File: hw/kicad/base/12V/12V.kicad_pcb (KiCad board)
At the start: 2 copper layers, 50 x 50 mm, 29 parts, among them J1 USB_B_Micro, J2 TOP, J3 XT60PW-M, J4 BUTTOM, U1 LM1117MP-3.3, U2 LM2596S-5, U3 CP2102N-Axx-xQFN28

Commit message: 修改尺寸至45x45
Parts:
- added D9: LED, LED_SMD:LED_0805_2012Metric, F.Cu at (83.0, 58.8)
- added JUMP1: 0, Resistor_SMD:R_01005_0402Metric, F.Cu at (71.7, 65.7)
- added R5: 10k, Resistor_SMD:R_0805_2012Metric, F.Cu at (80.3, 58.9)
- C1: footprint Capacitor_Tantalum_SMD:CP_EIA-3528-21_Kemet-B -> Capacitor_SMD:C_0805_2012Metric
- C10: value 10uF -> 47uF; footprint Capacitor_Tantalum_SMD:CP_EIA-3528-21_Kemet-B -> Capacitor_Tantalum_SMD:CP_EIA-3216-12_Kemet-S
- C2, C4, C5: footprint Capacitor_SMD:C_0603_1608Metric -> Capacitor_SMD:C_0805_2012Metric
- C6: footprint Capacitor_Tantalum_SMD:CP_EIA-3528-21_Kemet-B -> Capacitor_Tantalum_SMD:CP_EIA-6032-28_Kemet-C
- C9: value 10uF -> 0.1uF; footprint Capacitor_Tantalum_SMD:CP_EIA-3528-21_Kemet-B -> Capacitor_SMD:C_0805_2012Metric
- J1: footprint Connector_USB:USB_Micro-B_Molex_47346-0001 -> Connector_USB:USB_Micro-B_Wuerth_629105150521
- J3: value XT60PW-M -> XT30PW-M; footprint XT:XT60-PW-M -> XT:XT30-PAD
- R1, R2, R3, R4: footprint Resistor_SMD:R_0201_0603Metric -> Resistor_SMD:R_0805_2012Metric
- moved R1 25.0 mm to (83.0, 63.1), turned to 90 degrees
- moved R2 22.1 mm to (80.3, 63.1), turned to -90 degrees
- moved D1 17.5 mm to (78.9, 51.1), turned to -90 degrees
- moved U2 15.6 mm to (62.8, 39.8)
- moved D5 15.1 mm to (66.9, 59.2), turned to -90 degrees
- moved L1 14.8 mm to (79.9, 39.7)
- moved D6 12.1 mm to (69.5, 59.2), turned to -90 degrees
- moved J3 11.9 mm to (49.6, 45.4)
- moved C5 11.5 mm to (92.7, 43.4), turned to 90 degrees
- moved C8 11.1 mm to (62.1, 51.0)
- moved C4 10.8 mm to (74.9, 65.5), turned to 180 degrees
- moved C3 10.1 mm to (71.1, 50.9)
- moved C6 8.99 mm to (89.0, 41.7), turned to 90 degrees
- moved U1 8.47 mm to (89.8, 60.9)
- moved D8 8.13 mm to (85.1, 51.1), turned to 90 degrees
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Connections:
- C4 pad 2: VBUS -> Net-(U3-VBUS)
- J3 pad 1: +BATT -> GND
- J3 pad 2: GND -> +BATT
- U3 pad 7: VBUS -> Net-(U3-VBUS)
- U3 pad 8: VBUS -> Net-(U3-VBUS)
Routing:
- net /ADC_1: track 3.38 -> 36.9 mm
- net +BATT: track 78.4 -> 62.1 mm, vias 14 -> 10
- net +3.3V: track 33.5 -> 46.7 mm
- net /UART1_RX: track 36.7 -> 25.8 mm, vias 2 -> 3
- net Net-(D1-K): track 14.2 -> 21.5 mm
- net /UART1_TX: track 30.8 -> 23.8 mm, vias 2 -> 3
- net Net-(U3-VBUS): track 0.00 -> 6.70 mm
- net +5V: track 77.8 -> 72.6 mm, vias 4 -> 6
- net Net-(D8-A): track 33.0 -> 37.3 mm
- net Net-(D9-K): track 0.00 -> 2.74 mm
- net Net-(J1-D-): track 6.39 -> 8.70 mm
- net Net-(J1-D+): track 6.58 -> 5.15 mm
- net /USB-: track 28.5 -> 29.4 mm, vias 4 -> 2
- net /USB+: track 35.9 -> 36.3 mm, vias 3 -> 2
- net GND: vias 66 -> 40
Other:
- board size 50 x 50 mm -> 45 x 45 mm

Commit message: Pindar v1.0
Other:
- board text added: "Pindar v1.0 Type BASE 12V power v1.0"
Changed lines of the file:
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@@
     (property "ki_keywords" "R res resistor")
     (attr smd)
-    (fp_text reference "R5" (at 0.0544 0.0026 90) (layer "F.SilkS")
+    (fp_text reference "R5" (at 0.0544 0.0026 90) (layer "F.SilkS") hide
         (effects (font (size 1 1) (thickness 0.15)))
     )
@@
     (property "ki_keywords" "cap capacitor")
     (attr smd)
-    (fp_text reference "C5" (at 3.556 0 90) (layer "F.SilkS")
+    (fp_text reference "C5" (at 3.556 0 90) (layer "F.SilkS") hide
         (effects (font (size 1 1) (thickness 0.15)))
     )
@@
     (property "ki_keywords" "cap capacitor")
     (attr smd)
-    (fp_text reference "C2" (at -0.0808 -0.0074 180) (layer "F.SilkS")
+    (fp_text reference "C2" (at -0.0808 -0.0074 180) (layer "F.SilkS") hide
         (effects (font (size 1 1) (thickness 0.15)))
     )
@@
     (property "ki_keywords" "diode Schottky")
     (attr smd)
-    (fp_text reference "D8" (at -0.1016 -0.1016 180) (layer "F.SilkS")
+    (fp_text reference "D8" (at -0.1016 -0.1016 180) (layer "F.SilkS") hide
         (effects (font (size 1 1) (thickness 0.15)))
     )
@@
     (property "ki_keywords" "diode Schottky")
     (attr smd)
-    (fp_text reference "D7" (at -0.0508 -0.2032 90) (layer "F.SilkS")
+    (fp_text reference "D7" (at -0.0508 -0.2032 90) (layer "F.SilkS") hide
         (effects (font (size 1 1) (thickness 0.15)))
     )
@@
     (property "ki_keywords" "cap capacitor")
     (attr smd)
-    (fp_text reference "C6" (at 0 0.0508 90) (layer "F.SilkS")
+    (fp_text reference "C6" (at 0 0.0508 90) (layer "F.SilkS") hide
         (effects (font (size 1 1) (thickness 0.15)))
     )
@@
     (property "ki_keywords" "cap capacitor")
     (attr smd)
-    (fp_text reference "C10" (at -0.0212 0.0508 180) (layer "F.SilkS")
+    (fp_text reference "C10" (at -0.0212 0.0508 180) (layer "F.SilkS") hide
         (effects (font (size 1 1) (thickness 0.15)))
     )
@@
     (property "字段 4" "36V")
     (attr smd)
-    (fp_text reference "C3" (at 2.3952 -2.1172) (layer "F.SilkS")
+    (fp_text reference "C3" (at 2.3952 -2.1172) (layer "F.SilkS") hide
         (effects (font (size 1 1) (thickness 0.15)))
     )
@@
     (property "ki_keywords" "connector")
     (attr smd)
-    (fp_text reference "J2" (at 0 -13.76 90) (layer "F.SilkS")
+    (fp_text reference "J2" (at 0 -13.76 90) (layer "F.SilkS") hide
         (effects (font (size 1 1) (thickness 0.15)))
     )
@@
     (property "ki_keywords" "diode Schottky")
     (attr smd)
-    (fp_text reference "D3" (at -0.3216 -0.0762 -90) (layer "F.SilkS")
+    (fp_text reference "D3" (at -0.3216 -0.0762 -90) (layer "F.SilkS") hide
         (effects (font (size 1 1) (thickness 0.15)))
     )
@@
     (property "ki_keywords" "diode Schottky")
     (attr smd)
-    (fp_text reference "D6" (at -0.0225 -0.0762 90) (layer "F.SilkS")
+    (fp_text reference "D6" (at -0.0225 -0.0762 90) (layer "F.SilkS") hide
         (effects (font (size 1 1) (thickness 0.15)))
     )
@@
     (property "ki_keywords" "LED diode")
     (attr smd)
-    (fp_text reference "D9" (at -0.1755 -0.067 90) (layer "F.SilkS")
+    (fp_text reference "D9" (at -0.1755 -0.067 90) (layer "F.SilkS") hide
         (effects (font (size 1 1) (thickness 0.15)))
     )
@@
     (property "ki_keywords" "diode Schottky")
     (attr smd)
-    (fp_text reference "D4" (at -0.22 -0.0762 90) (layer "F.SilkS")
+    (fp_text reference "D4" (at -0.22 -0.0762 90) (layer "F.SilkS") hide
         (effects (font (size 1 1) (thickness 0.15)))
     )
@@
     (property "ki_keywords" "inductor choke coil reactor magnetic")
     (attr smd)
-    (fp_text reference "L1" (at -0.0398 0.145 90) (layer "F.SilkS")
+    (fp_text reference "L1" (at -0.0398 0.145 90) (layer "F.SilkS") hide
         (effects (font (size 1 1) (thickness 0.15)))
     )
@@
     (property "ki_keywords" "R res resistor")
     (attr smd)
-    (fp_text reference "R2" (at 0.0508 0 90) (layer "F.SilkS")
+    (fp_text reference "R2" (at 0.0508 0 90) (layer "F.SilkS") hide
         (effects (font (size 1 1) (thickness 0.15)))
     )
@@
     (property "ki_keywords" "diode Schottky")
     (attr smd)
-    (fp_text reference "D2" (at -0.2708 -0.0508 90) (layer "F.SilkS")
+    (fp_text reference "D2" (at -0.2708 -0.0508 90) (layer "F.SilkS") hide
         (effects (font (size 1 1) (thickness 0.15)))
     )
@@
     (property "ki_keywords" "USB UART bridge")
     (attr smd)
-    (fp_text reference "U3" (at 0 -3.8) (layer "F.SilkS")
+    (fp_text reference "U3" (at 0 -3.8) (layer "F.SilkS") hide
         (effects (font (size 1 1) (thickness 0.15)))
     )
@@
     (property "ki_keywords" "cap capacitor")
     (attr smd)
-    (fp_text reference "C4" (at -1.5138 -0.0508) (layer "F.SilkS")
+    (fp_text reference "C4" (at -1.5138 -0.0508) (layer "F.SilkS") hide
         (effects (font (size 1 1) (thickness 0.15)))
     )
@@
     (property "ki_keywords" "linear regulator ldo fixed positive")
     (attr smd)
-    (fp_text reference "U1" (at 0.1016 -0.1524) (layer "F.SilkS")
+    (fp_text reference "U1" (at 0.1016 -0.1524) (layer "F.SilkS") hide
         (effects (font (size 1 1) (thickness 0.15)))
     )
@@
     (property "ki_keywords" "diode Schottky")
     (attr smd)
-    (fp_text reference "D1" (at 0.0566 -0.1524 -180) (layer "F.SilkS")
+    (fp_text reference "D1" (at 0.0566 -0.1524 -180) (layer "F.SilkS") hide
         (effects (font (size 1 1) (thickness 0.15)))
     )
@@
     (property "ki_keywords" "cap capacitor")
     (attr smd)
-    (fp_text reference "C1" (at 0.1856 0.0336 90) (layer "F.SilkS")
+    (fp_text reference "C1" (at 0.1856 0.0336 90) (layer "F.SilkS") hide
         (effects (font (size 1 1) (thickness 0.15)))
     )
@@
     (property "ki_keywords" "R res resistor")
     (attr smd)
-    (fp_text reference "R1" (at 0.0508 -0.0092 90) (layer "F.SilkS")
+    (fp_text reference "R1" (at 0.0508 -0.0092 90) (layer "F.SilkS") hide
         (effects (font (size 1 1) (thickness 0.15)))
     )
@@
     (property "ki_keywords" "Step-Down Voltage Regulator 5V 3A")
     (attr smd)
-    (fp_text reference "U2" (at -4.1956 0.0272) (layer "F.SilkS")
+    (fp_text reference "U2" (at -4.1956 0.0272) (layer "F.SilkS") hide
         (effects (font (size 1 1) (thickness 0.15)))
     )
@@
     (property "字段 4" "30V")
     (attr smd)
-    (fp_text reference "C8" (at 2.446 -2.1172 -180) (layer "F.SilkS")
+    (fp_text reference "C8" (at 2.446 -2.1172 -180) (layer "F.SilkS") hide
         (effects (font (size 1 1) (thickness 0.15)))
     )
@@
     (property "ki_keywords" "R res resistor")
     (attr smd)
-    (fp_text reference "R4" (at -0.0575 -0.067734 90) (layer "F.SilkS")
+    (fp_text reference "R4" (at -0.0575 -0.067734 90) (layer "F.SilkS") hide
         (effects (font (size 1 1) (thickness 0.15)))
     )
@@
     (property "ki_keywords" "R res resistor")
     (attr smd)
-    (fp_text reference "R3" (at 0.0695 -0.0254 90) (layer "F.SilkS")
+    (fp_text reference "R3" (at 0.0695 -0.0254 90) (layer "F.SilkS") hide
         (effects (font (size 1 1) (thickness 0.15)))
     )
@@
     (property "ki_keywords" "connector USB micro")
     (attr smd)
-    (fp_text reference "J1" (at 0.259 1.3646 -90) (layer "F.SilkS")
+    (fp_text reference "J1" (at 0.259 1.3646 -90) (layer "F.SilkS") hide
         (effects (font (size 1 1) (thickness 0.15)))
     )
@@
     (property "ki_keywords" "cap capacitor")
     (attr smd)
-    (fp_text reference "C9" (at 3.1492 -0.0508 180) (layer "F.SilkS")
+    (fp_text reference "C9" (at 3.1492 -0.0508 180) (layer "F.SilkS") hide
         (effects (font (size 1 1) (thickness 0.15)))
     )
@@
     (property "ki_keywords" "diode Schottky")
     (attr smd)
-    (fp_text reference "D5" (at 0 -0.160868 90) (layer "F.SilkS")
+    (fp_text reference "D5" (at 0 -0.160868 90) (layer "F.SilkS") hide
         (effects (font (size 1 1) (thickness 0.15)))
     )
@@
     (property "ki_keywords" "connector")
     (attr smd)
-    (fp_text reference "J4" (at 0 13.76 90) (layer "B.SilkS")
+    (fp_text reference "J4" (at 0 13.76 90) (layer "B.SilkS") hide
         (effects (font (size 1 1) (thickness 0.15)) (justify mirror))
     )
@@
   (gr_circle (center 73.22 72.22) (end 74.22 72.22)
     (stroke (width 0.15) (type default)) (fill none) (layer "User.1"))
+  (gr_text "Pindar v1.0 \nType BASE\n12V power v1.0" (at 84.396 41.0796) (layer "B.SilkS")
+    (effects (font (size 1 1) (thickness 0.15)) (justify left bottom mirror))
+  )
   (segment (start 92.9136 60.8584) (end 86.6136 60.8584) (width 0.762) (layer "F.Cu") (net 1))
   (segment (start 90.3144 68.8644) (end 91.282 69.832) (width 0.762) (layer "F.Cu") (net 1))

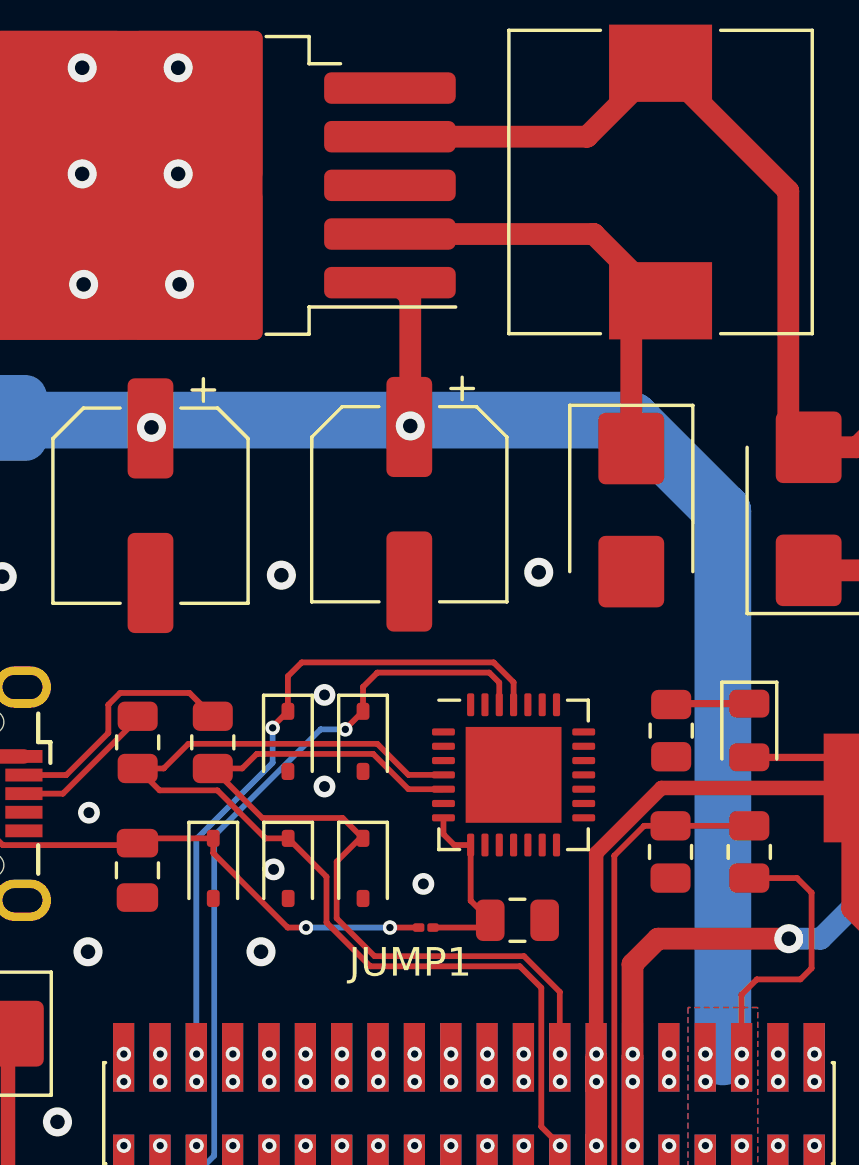
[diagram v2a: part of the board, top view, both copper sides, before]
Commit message: 第二次打样的整改；dc motor改成了三路 io不够做不了四路；
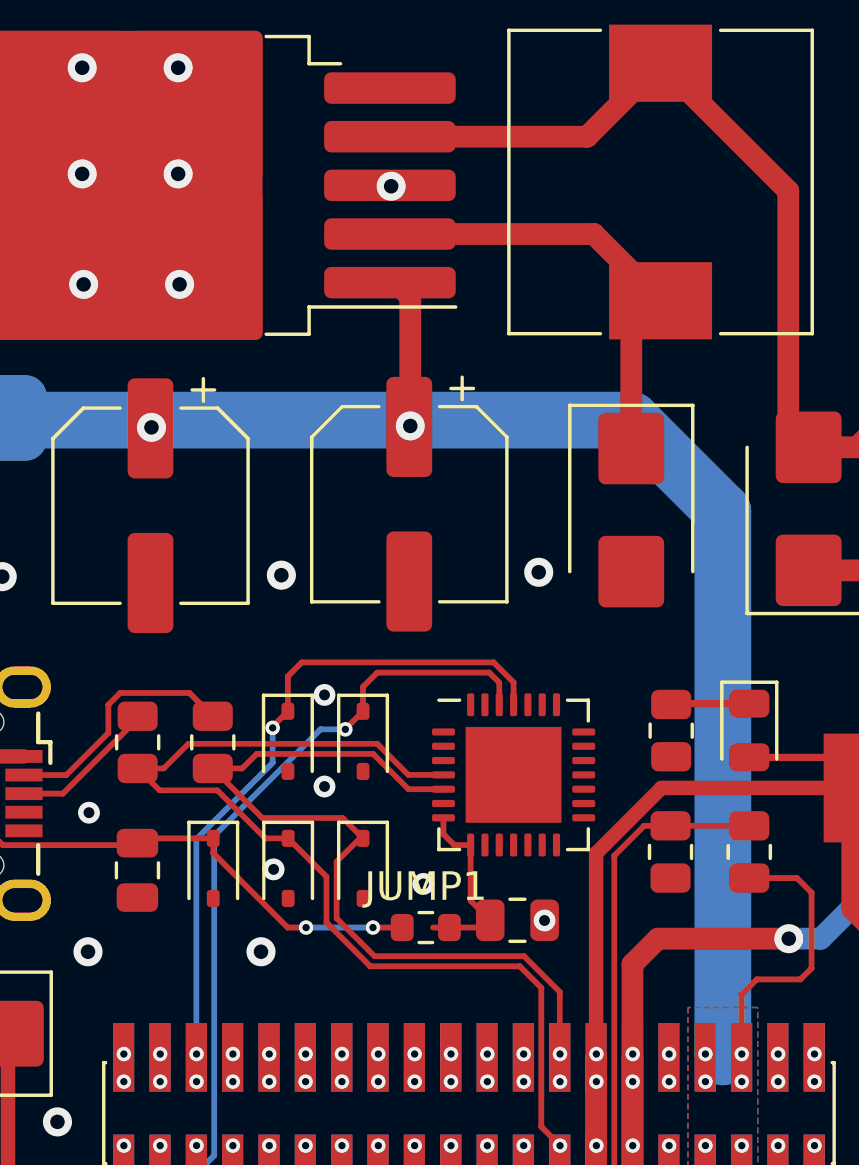
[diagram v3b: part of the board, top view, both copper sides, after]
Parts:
- JUMP1: footprint Resistor_SMD:R_01005_0402Metric -> Resistor_SMD:R_0603_1608Metric
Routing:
- net VBUS: track 35.3 -> 34.8 mm
- net GND: vias 40 -> 42
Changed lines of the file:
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@@
     )
   )
-  (footprint "Resistor_SMD:R_01005_0402Metric" (layer "F.Cu")
+  (footprint "Resistor_SMD:R_0603_1608Metric" (layer "F.Cu")
     (at 71.7144 65.7352)
-    (descr "Resistor SMD 01005 (0402 Metric), square (rectangular) end terminal, IPC_7351 nominal, (Body size source: http://www.vishay.com/docs/20056/crcw01005e3.pdf), generated with kicad-footprint-generator")
+    (descr "Resistor SMD 0603 (1608 Metric), square (rectangular) end terminal, IPC_7351 nominal, (Body size source: IPC-SM-782 page 72, https://www.pcb-3d.com/wordpress/wp-content/uploads/ipc-sm-782a_amendment_1_and_2.pdf), generated with kicad-footprint-generator")
     (tags "resistor")
     (property "Sheetfile" "12V.kicad_sch")
@@
     (property "ki_keywords" "R res resistor")
     (attr smd)
-    (fp_text reference "JUMP1" (at -0.5436 1.2192) (layer "F.SilkS")
+    (fp_text reference "JUMP1" (at 0 -1.43) (layer "F.SilkS")
         (effects (font (size 1 1) (thickness 0.15)))
     )
-    (fp_text value "0" (at 0 1) (layer "F.Fab")
+    (fp_text value "0" (at 0 1.43) (layer "F.Fab")
         (effects (font (size 1 1) (thickness 0.15)))
     )
-    (fp_text user "${REFERENCE}" (at 0 -0.62) (layer "F.Fab")
-        (effects (font (size 0.25 0.25) (thickness 0.04)))
-    )
-    (fp_line (start -0.6 -0.3) (end 0.6 -0.3)
+    (fp_text user "${REFERENCE}" (at 0 0) (layer "F.Fab")
+        (effects (font (size 0.4 0.4) (thickness 0.06)))
+    )
+    (fp_line (start -0.237258 -0.5225) (end 0.237258 -0.5225)
+      (stroke (width 0.12) (type solid)) (layer "F.SilkS"))
+    (fp_line (start -0.237258 0.5225) (end 0.237258 0.5225)
+      (stroke (width 0.12) (type solid)) (layer "F.SilkS"))
+    (fp_line (start -1.48 -0.73) (end 1.48 -0.73)
       (stroke (width 0.05) (type solid)) (layer "F.CrtYd"))
-    (fp_line (start -0.6 0.3) (end -0.6 -0.3)
+    (fp_line (start -1.48 0.73) (end -1.48 -0.73)
       (stroke (width 0.05) (type solid)) (layer "F.CrtYd"))
-    (fp_line (start 0.6 -0.3) (end 0.6 0.3)
+    (fp_line (start 1.48 -0.73) (end 1.48 0.73)
       (stroke (width 0.05) (type solid)) (layer "F.CrtYd"))
-    (fp_line (start 0.6 0.3) (end -0.6 0.3)
+    (fp_line (start 1.48 0.73) (end -1.48 0.73)
       (stroke (width 0.05) (type solid)) (layer "F.CrtYd"))
-    (fp_line (start -0.2 -0.1) (end 0.2 -0.1)
-      (stroke (width 0.1) (type solid)) (layer "F.Fab"))
-    (fp_line (start -0.2 0.1) (end -0.2 -0.1)
-      (stroke (width 0.1) (type solid)) (layer "F.Fab"))
-    (fp_line (start 0.2 -0.1) (end 0.2 0.1)
-      (stroke (width 0.1) (type solid)) (layer "F.Fab"))
-    (fp_line (start 0.2 0.1) (end -0.2 0.1)
-      (stroke (width 0.1) (type solid)) (layer "F.Fab"))
-    (pad "" smd roundrect (at -0.275 0) (size 0.27 0.27) (layers "F.Paste") (roundrect_rratio 0.25))
-    (pad "" smd roundrect (at 0.275 0) (size 0.27 0.27) (layers "F.Paste") (roundrect_rratio 0.25))
-    (pad "1" smd roundrect (at -0.25 0) (size 0.4 0.3) (layers "F.Cu" "F.Mask") (roundrect_rratio 0.25)
+    (fp_line (start -0.8 -0.4125) (end 0.8 -0.4125)
+      (stroke (width 0.1) (type solid)) (layer "F.Fab"))
+    (fp_line (start -0.8 0.4125) (end -0.8 -0.4125)
+      (stroke (width 0.1) (type solid)) (layer "F.Fab"))
+    (fp_line (start 0.8 -0.4125) (end 0.8 0.4125)
+      (stroke (width 0.1) (type solid)) (layer "F.Fab"))
+    (fp_line (start 0.8 0.4125) (end -0.8 0.4125)
+      (stroke (width 0.1) (type solid)) (layer "F.Fab"))
+    (pad "1" smd roundrect (at -0.825 0) (size 0.8 0.95) (layers "F.Cu" "F.Paste" "F.Mask") (roundrect_rratio 0.25)
       (net 28 "VBUS") (pintype "passive"))
-    (pad "2" smd roundrect (at 0.25 0) (size 0.4 0.3) (layers "F.Cu" "F.Mask") (roundrect_rratio 0.25)
+    (pad "2" smd roundrect (at 0.825 0) (size 0.8 0.95) (layers "F.Cu" "F.Paste" "F.Mask") (roundrect_rratio 0.25)
       (net 59 "Net-(U3-VBUS)") (pintype "passive"))
-    (model "${KICAD6_3DMODEL_DIR}/Resistor_SMD.3dshapes/R_01005_0402Metric.wrl"
+    (model "${KICAD6_3DMODEL_DIR}/Resistor_SMD.3dshapes/R_0603_1608Metric.wrl"
       (offset (xyz 0 0 0))
       (scale (xyz 1 1 1))
@@
   (via (at 88.4092 71.204) (size 1.016) (drill 0.508) (layers "F.Cu" "B.Cu") (net 2))
   (via (at 88.0536 55.8116) (size 1.016) (drill 0.508) (layers "F.Cu" "B.Cu") (net 2))
+  (via (at 70.5022 39.835) (size 1.016) (drill 0.508) (layers "F.Cu" "B.Cu") (net 2))
   (via (at 66.3956 63.7032) (size 0.762) (drill 0.381) (layers "F.Cu" "B.Cu") (net 2))
   (via (at 84.0232 73.3552) (size 0.508) (drill 0.254) (layers "F.Cu" "B.Cu") (net 2))
@@
   (via (at 85.2932 74.3204) (size 0.508) (drill 0.254) (layers "F.Cu" "B.Cu") (net 2))
   (via (at 80.2132 71.12) (size 0.508) (drill 0.254) (layers "F.Cu" "B.Cu") (net 2))
+  (via (at 75.8616 65.489) (size 0.762) (drill 0.381) (layers "F.Cu" "B.Cu") (net 2))
   (via (at 84.0232 74.3204) (size 0.508) (drill 0.254) (layers "F.Cu" "B.Cu") (net 2))
   (via (at 55.5498 39.4208) (size 1.016) (drill 0.508) (layers "F.Cu" "B.Cu") (net 2))
@@
   (via (at 76.4032 73.3552) (size 0.508) (drill 0.254) (layers "F.Cu" "B.Cu") (net 27))
   (segment (start 61.569861 62.854139) (end 56.931861 62.854139) (width 0.2032) (layer "F.Cu") (net 28))
+  (segment (start 70.8894 65.7352) (end 69.867208 65.7352) (width 0.2032) (layer "F.Cu") (net 28))
   (segment (start 53.6794 59.7566) (end 51.884 61.552) (width 0.508) (layer "F.Cu") (net 28))
-  (segment (start 71.4644 65.7352) (end 70.459228 65.7352) (width 0.2032) (layer "F.Cu") (net 28))
   (segment (start 56.4388 60.136) (end 56.8182 59.7566) (width 0.2032) (layer "F.Cu") (net 28))
   (segment (start 64.2874 62.6192) (end 61.8048 62.6192) (width 0.2032) (layer "F.Cu") (net 28))
   (segment (start 56.4388 62.361078) (end 56.4388 60.136) (width 0.2032) (layer "F.Cu") (net 28))
+  (segment (start 69.867208 65.7352) (end 69.8672 65.735192) (width 0.2032) (layer "F.Cu") (net 28))
   (segment (start 61.8048 62.6192) (end 61.6376 62.7864) (width 0.2032) (layer "F.Cu") (net 28))
   (segment (start 56.931861 62.854139) (end 56.4388 62.361078) (width 0.2032) (layer "F.Cu") (net 28))
   (segment (start 51.884 61.552) (end 51.884 68.512) (width 0.508) (layer "F.Cu") (net 28))
-  (segment (start 70.459228 65.7352) (end 70.45922 65.735192) (width 0.2032) (layer "F.Cu") (net 28))
   (segment (start 64.2874 63.135) (end 66.887592 65.735192) (width 0.2032) (layer "F.Cu") (net 28))
   (segment (start 51.884 68.512) (end 52.8156 69.4436) (width 0.508) (layer "F.Cu") (net 28))
@@
   (segment (start 56.8182 59.7566) (end 57.6714 59.7566) (width 0.2032) (layer "F.Cu") (net 28))
   (via (at 67.5304 65.735192) (size 0.508) (drill 0.254) (layers "F.Cu" "B.Cu") (net 28))
-  (via (at 70.45922 65.735192) (size 0.508) (drill 0.254) (layers "F.Cu" "B.Cu") (net 28))
-  (segment (start 70.45922 65.735192) (end 67.5304 65.735192) (width 0.2032) (layer "B.Cu") (net 28))
+  (via (at 69.8672 65.735192) (size 0.508) (drill 0.254) (layers "F.Cu" "B.Cu") (net 28))
+  (segment (start 69.8672 65.735192) (end 67.5304 65.735192) (width 0.2032) (layer "B.Cu") (net 28))
   (segment (start 70.4596 43.2036) (end 70.6864 43.2036) (width 0.762) (layer "F.Cu") (net 29))
   (segment (start 84.6817 64.0061) (end 83.0164 64.0061) (width 0.2032) (layer "F.Cu") (net 29))
